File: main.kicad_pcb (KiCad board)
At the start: 2 copper layers, 124 parts, among them J1 Conn_Debug, J10 FC_D_NC, J11 FC_D_NC, J12 P0, J13 V0, J14 Conn_free, J15 Conn_01x09, J2 CAN_conn, J3 CAN_conn, J4 Conn_Power_In, J5 Conn_Power_In, J6 AX0, J7 AX1, J8 AX2, J9 stepper, Q1 BSS138, Q10 IRF540N, Q11 BSS138, Q12 BSS138, Q13 BSS138, Q14 BSS138, Q15 BSS138, Q16 BSS138, Q2 BSS138, Q3 BSS138, Q4 BSS138, Q5 BSS138, Q6 BSS138, Q7 BSS138, Q8 BSS138, Q9 IRF540N, U1 TCAN332, U2 LD1117S50TR_SOT223, U3 LD1117S33TR_SOT223, U4 74LS126, U5 MC34152, U6 MPXA6115A, U7 STM32F303K8Tx

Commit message: first layout
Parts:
- added H1: MountingHole_Pad, MountingHole:MountingHole_3.2mm_M3_Pad, F.Cu at (190.5, 44.5)
- added H2: MountingHole_Pad, MountingHole:MountingHole_3.2mm_M3_Pad, F.Cu at (99.1, 105.4)
- added H3: MountingHole_Pad, MountingHole:MountingHole_3.2mm_M3_Pad, F.Cu at (99.1, 44.5)
- added H4: MountingHole_Pad, MountingHole:MountingHole_3.2mm_M3_Pad, F.Cu at (190.5, 105.4)
- C18, C21, C3, D11, D5, D6, Q11, Q13, Q15, Q5, Q6, Q7, Q8, R15, R16, R17, R18, R19, R22, R23, R26, R27, R30, R31, R34, R35, U5: moved to B.Cu
- moved Q7 94.2 mm to (108.0, 99.1)
- moved Q6 90.9 mm to (104.1, 93.3)
- moved R15 90.7 mm to (104.4, 102.9)
- moved Q8 88.4 mm to (107.8, 93.3)
- moved Q5 87.3 mm to (104.1, 99.1)
- moved R17 85.3 mm to (109.0, 102.9), turned to 180 degrees
- moved R12 83.8 mm to (136.1, 81.3)
- moved R9 82.1 mm to (132.1, 76.2), turned to 90 degrees
- moved R16 81.7 mm to (103.1, 88.9)
- moved R18 77.8 mm to (107.7, 88.9), turned to 180 degrees
- moved R19 76.5 mm to (111.8, 95.0), turned to 90 degrees
- moved Q3 73.5 mm to (137.2, 76.2)
- moved Q4 68.5 mm to (156.2, 76.2)
- moved R13 68.2 mm to (156.5, 82.5)
- moved C13 65.5 mm to (150.9, 82.5), turned to 180 degrees
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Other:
- board outline added: 100 x 69 mm

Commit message: routing done
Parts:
- added C12: 100u, Capacitor_SMD:CP_Elec_4x5.4, F.Cu at (134.0, 69.0)
- C14: moved to B.Cu
- moved C22 47.2 mm to (161.5, 97.5), turned to 180 degrees
- moved C24 26.5 mm to (143.9, 91.1), turned to 90 degrees
- moved R24 20.3 mm to (147.0, 105.0)
- moved J14 17.8 mm to (166.0, 101.5)
- moved C23 16.0 mm to (162.9, 93.4), turned to 90 degrees
- moved C1 15.1 mm to (131.0, 92.0), turned to 270 degrees
- moved C26 13.6 mm to (155.3, 102.5), turned to 180 degrees
- moved C25 11.7 mm to (160.4, 93.4), turned to 270 degrees
- moved JP4 10.3 mm to (128.5, 105.0)
- moved U7 9.48 mm to (151.5, 94.9), turned to 180 degrees
- moved D13 7.65 mm to (128.7, 100.1)
- moved R25 7.65 mm to (133.5, 100.1)
- moved C2 6.32 mm to (134.7, 92.0)
- moved C4 6.32 mm to (127.3, 85.9)
- moved C5 6.32 mm to (127.3, 91.0)
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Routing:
- net GND: track 0.00 -> 637.2 mm, vias 0 -> 15
- net +3V3: track 0.00 -> 385.4 mm, vias 0 -> 20
- net +5V: track 0.00 -> 250.8 mm, vias 0 -> 16
- net /power_regul/PUMP_POWER: track 0.00 -> 116.2 mm, vias 0 -> 4
- net Net-(C5-Pad1): track 0.00 -> 81.2 mm, vias 0 -> 1
- net Net-(C4-Pad2): track 0.00 -> 76.1 mm, vias 0 -> 1
- net /stepper/STEP: track 0.00 -> 73.0 mm, vias 0 -> 5
- net /reset_logic/Reset_MCU: track 0.00 -> 70.1 mm, vias 0 -> 5
- net /stepper/DIR: track 0.00 -> 55.1 mm, vias 0 -> 3
- net /f3/ADC1_IN2: track 0.00 -> 54.6 mm, vias 0 -> 3
- net /color/LED: track 0.00 -> 54.6 mm, vias 0 -> 2
- net /color/OUT: track 0.00 -> 53.1 mm, vias 0 -> 3
- net /f3/FC_D: track 0.00 -> 51.0 mm, vias 0 -> 2
- net /color/S2: track 0.00 -> 49.5 mm, vias 0 -> 3
- net /power_regul/AX_POWER: track 0.00 -> 49.5 mm
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- added copper zone on B.Cu, net GND
- added copper zone on F.Cu, net GND

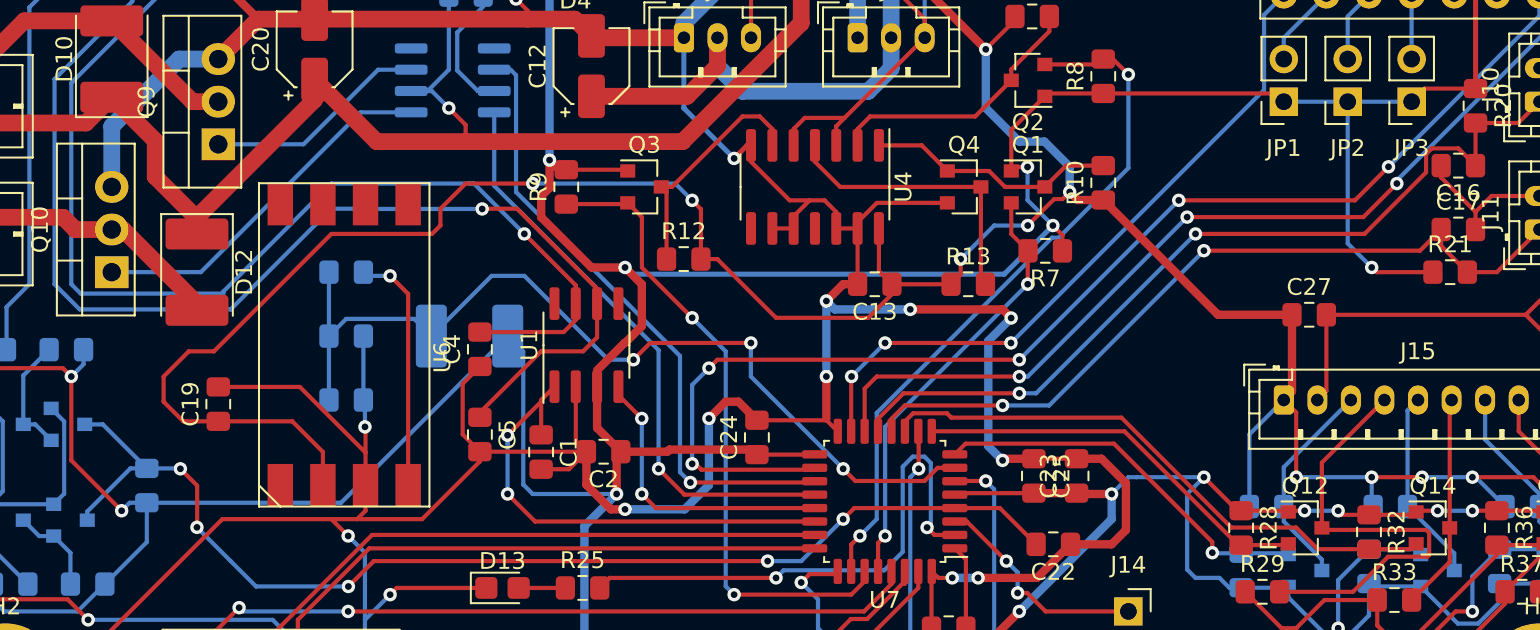
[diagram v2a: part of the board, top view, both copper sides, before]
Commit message: changing pump sensor
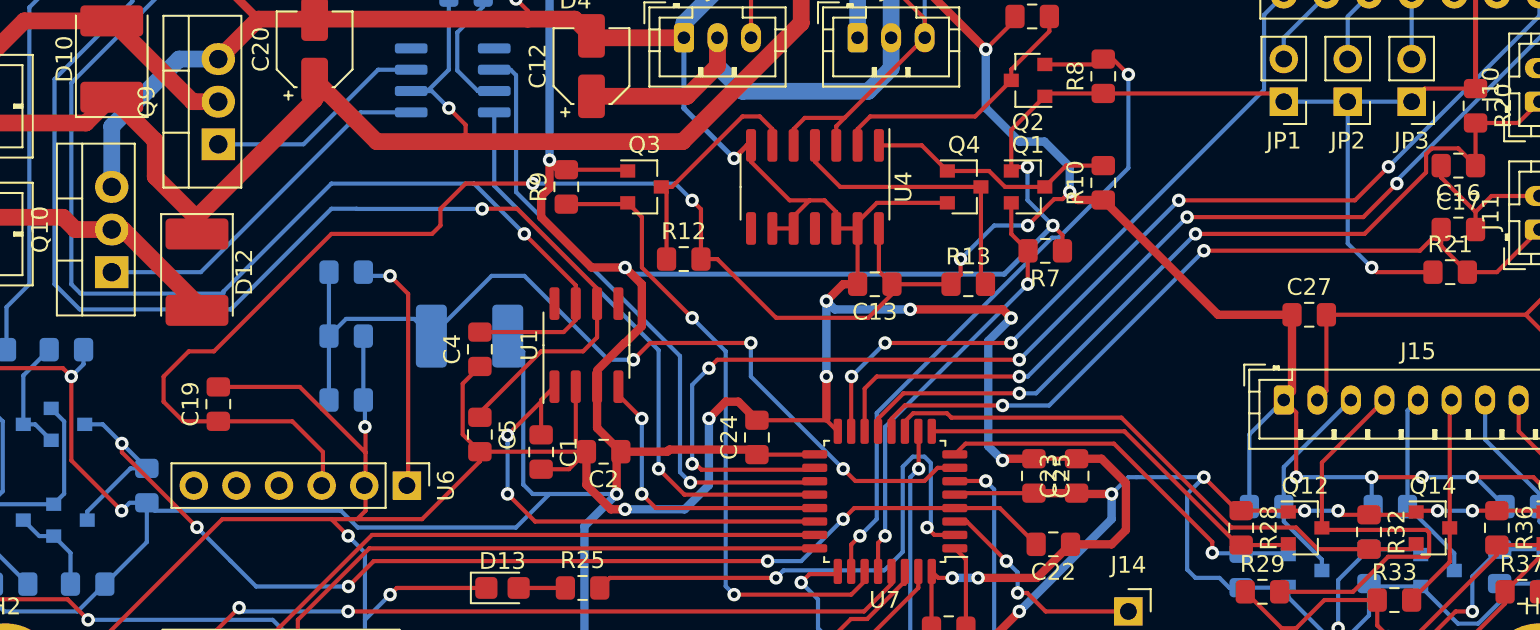
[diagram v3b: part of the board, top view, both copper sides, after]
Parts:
- JP1, JP2, JP3: footprint Connector_PinSocket_2.54mm:PinSocket_1x02_P2.54mm_Vertical -> Connector_PinHeader_2.54mm:PinHeader_1x02_P2.54mm_Vertical
- U6: value MPXA6115A -> MPX5500DP; footprint sensors:MPXA6115A -> Connector_PinHeader_2.54mm:PinHeader_1x06_P2.54mm_Vertical
- moved U6 2.62 mm to (123.0, 94.0)
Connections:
- U6 pad 1: Net-(U6-Pad1) -> Net-(R22-Pad2)
- U6 pad 2: +5V -> GND
- U6 pad 3: GND -> +5V
- U6 pad 4: Net-(R22-Pad2) -> Net-(U6-Pad4)
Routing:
- net /reset_logic/Reset_MCU: track 70.1 -> 71.1 mm

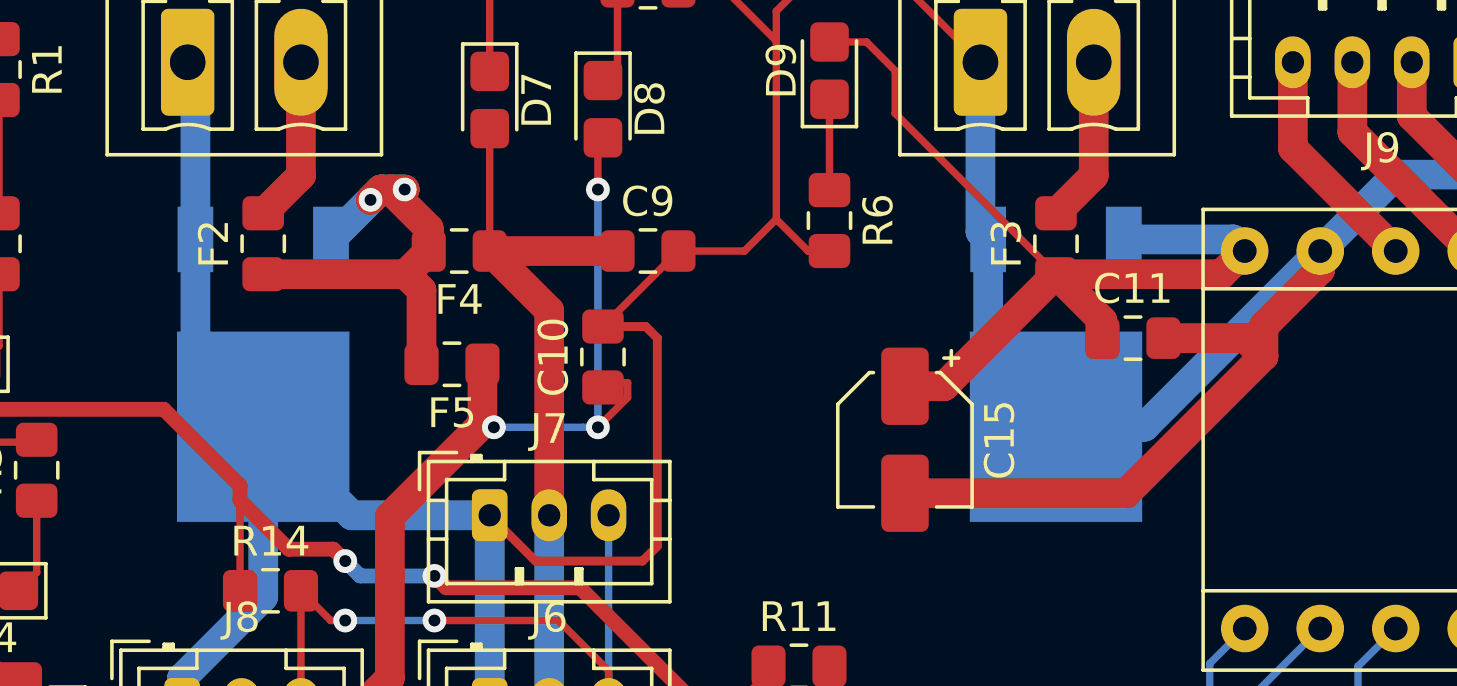
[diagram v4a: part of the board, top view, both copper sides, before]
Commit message: bigger fuses
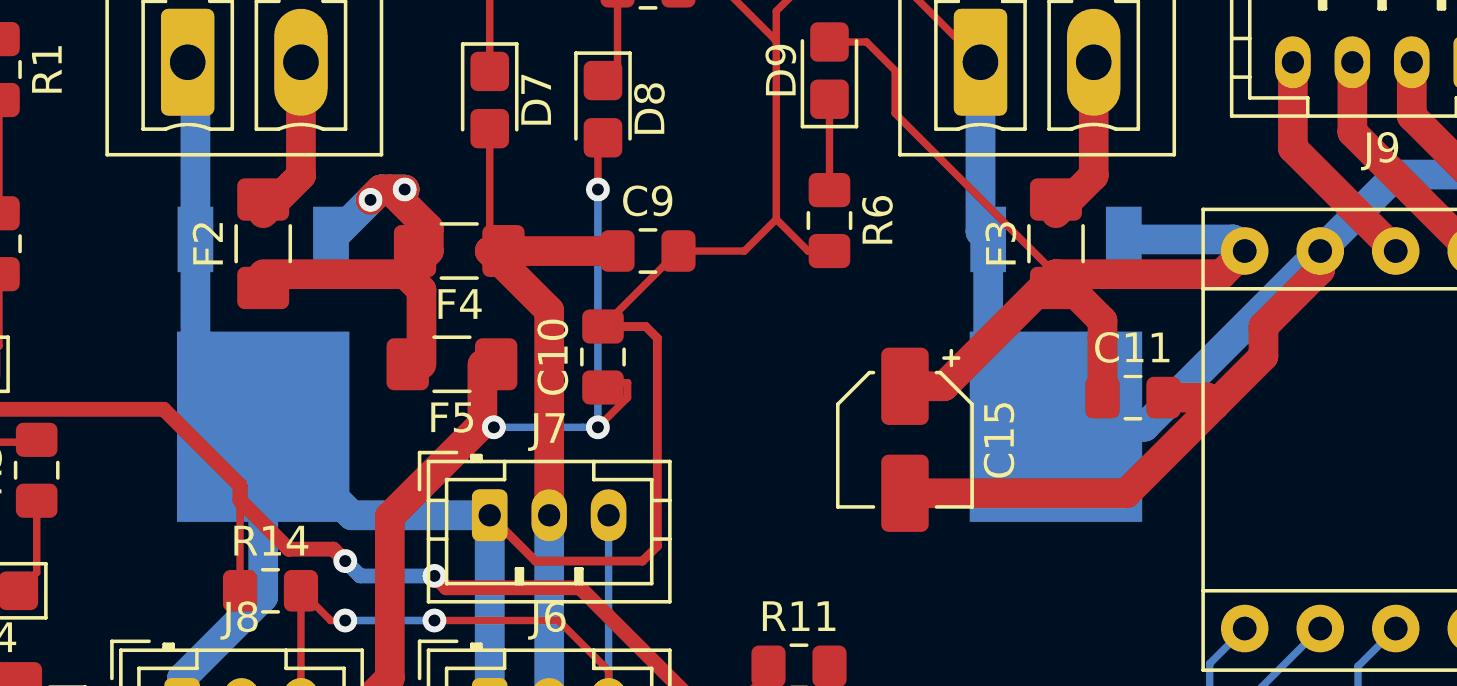
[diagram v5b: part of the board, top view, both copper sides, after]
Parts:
- F2, F3, F4, F5: footprint Fuse:Fuse_0805_2012Metric_Pad1.15x1.40mm_HandSolder -> Fuse:Fuse_1206_3216Metric_Pad1.42x1.75mm_HandSolder
- moved C11 2.00 mm to (171.5, 57.0)
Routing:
- net /power_regul/STEPPER_POWER: track 32.0 -> 34.0 mm
- net GND: track 637.2 -> 635.4 mm

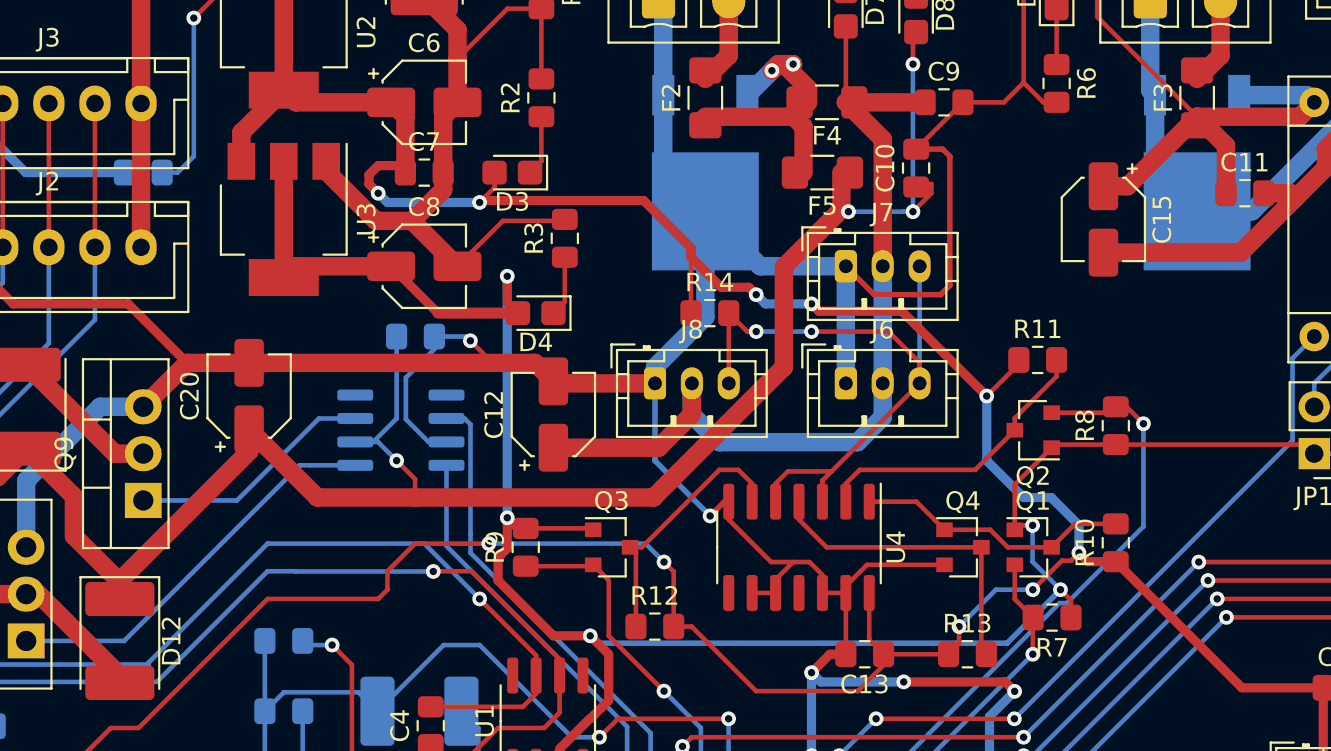
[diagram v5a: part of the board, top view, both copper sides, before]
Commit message: cap size rectification
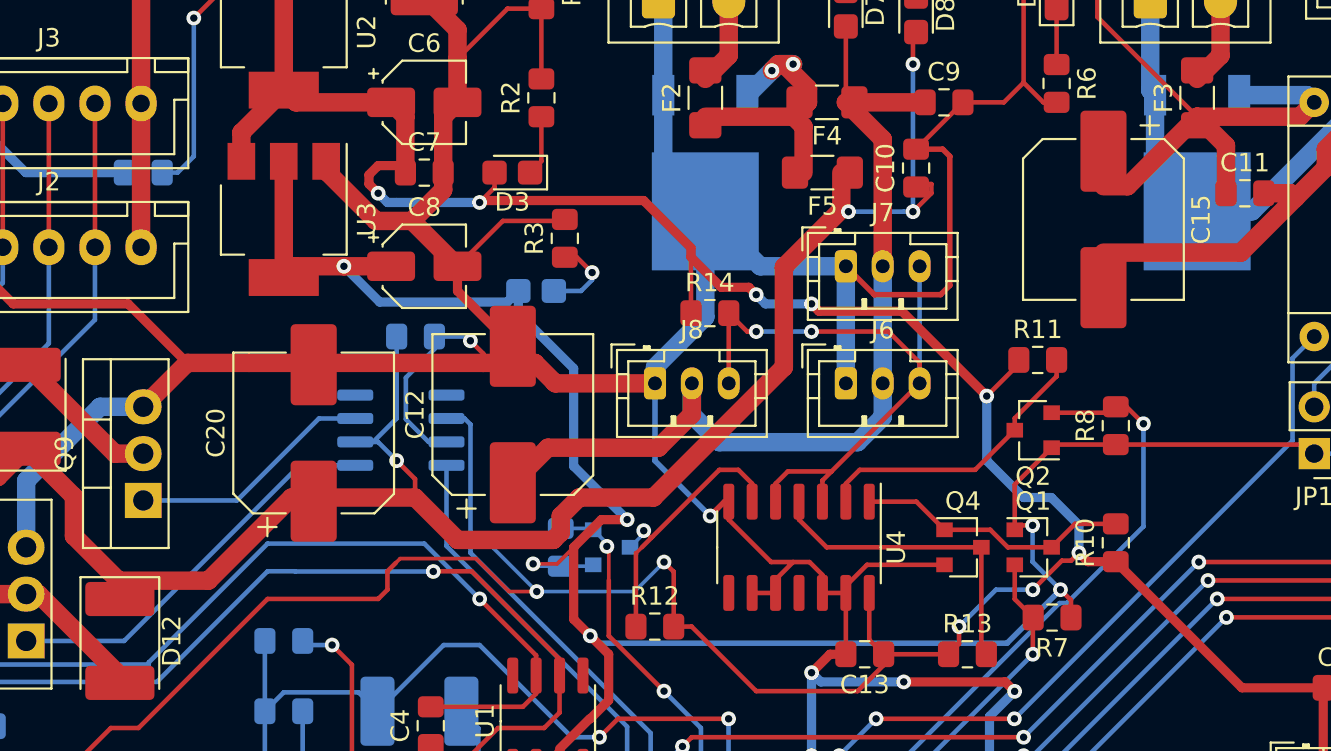
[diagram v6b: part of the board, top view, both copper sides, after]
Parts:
- C12, C15, C20: footprint Capacitor_SMD:CP_Elec_4x5.4 -> Capacitor_SMD:CP_Elec_8x10.5
- D4, Q3, R9: moved to B.Cu
- moved C20 4.03 mm to (121.0, 70.0)
- moved C12 2.20 mm to (131.8, 69.0)
- moved R9 1.90 mm to (134.4, 76.2), turned to 270 degrees
- moved D4 1.20 mm to (133.1, 62.3)
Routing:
- net GND: track 635.4 -> 641.0 mm
- net +5V: track 250.8 -> 255.1 mm
- net /power_regul/AX_POWER: track 49.5 -> 51.9 mm
- net +3V3: track 385.2 -> 387.4 mm, vias 20 -> 21
- net /power_regul/PUMP_POWER: track 116.2 -> 114.9 mm
- net Net-(D4-Pad1): track 3.28 -> 4.55 mm, vias 0 -> 1
- net Net-(Q3-Pad3): track 14.1 -> 15.2 mm, vias 0 -> 1
- net /AX12/RX: vias 2 -> 3
